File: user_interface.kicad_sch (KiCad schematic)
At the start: 31 parts, among them CN5 Line out, CN6 Headphone, J2 SWD, J3 I2C, J6 SPI, J9 Serial, P1 GPIO, SW4 BTN1, SW5 BTN2

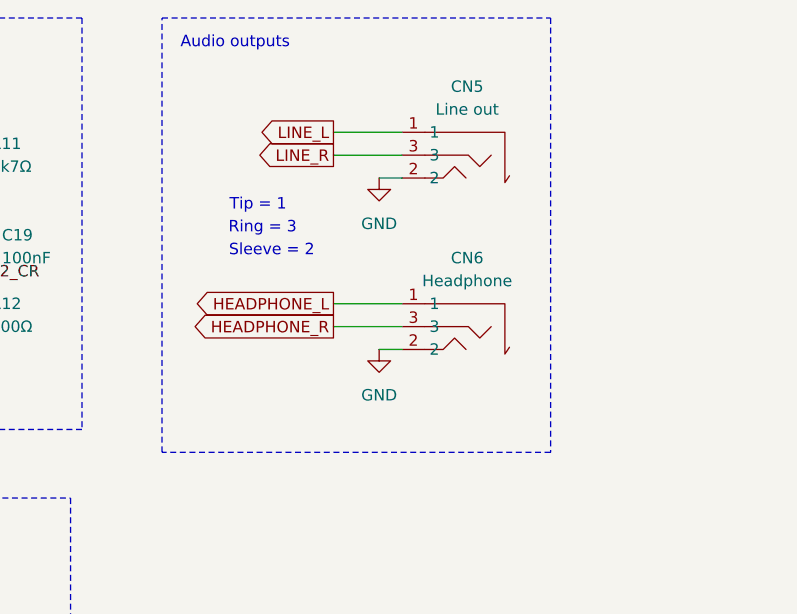
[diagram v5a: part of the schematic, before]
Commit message: Wire in headphone jack with 0-ohm
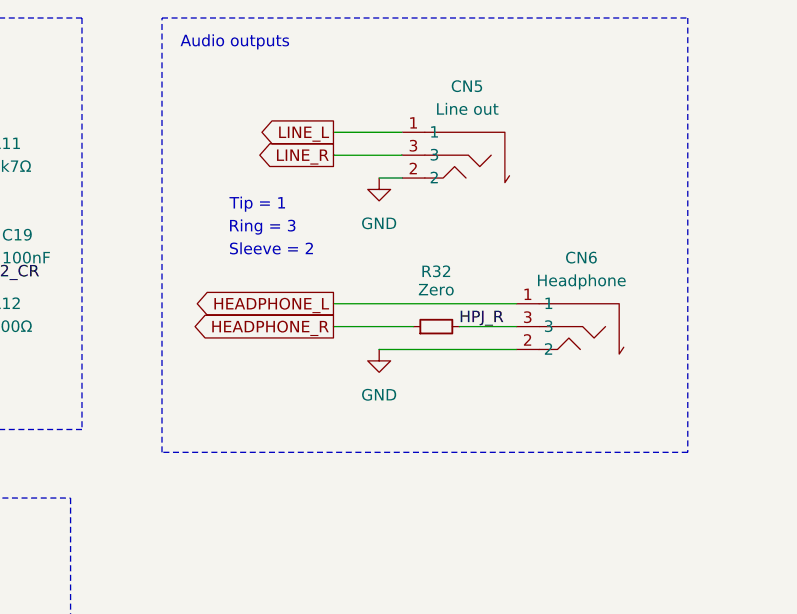
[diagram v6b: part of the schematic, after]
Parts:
- added R32: Zero, Resistor_SMD:R_2010_5025Metric, symbol Device:R_Small
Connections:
- net HEADPHONE_R: now also R32.1; no longer CN6.3
- new net HPJ_R: CN6.3, R32.2
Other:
- moved on the sheet: CN6
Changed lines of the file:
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@@
 	(wire
 		(pts
-			(xy 212.09 53.34) (xy 219.71 53.34)
+			(xy 212.09 53.34) (xy 220.98 53.34)
 		)
 		(stroke
@@
 	(wire
 		(pts
+			(xy 226.06 53.34) (xy 232.41 53.34)
+		)
+		(stroke
+			(width 0)
+			(type default)
+		)
+	)
+	(wire
+		(pts
 			(xy 68.58 175.26) (xy 74.93 175.26)
 		)
@@
 	(wire
 		(pts
-			(xy 212.09 50.8) (xy 219.71 50.8)
+			(xy 212.09 50.8) (xy 232.41 50.8)
 		)
 		(stroke
@@
 	(wire
 		(pts
-			(xy 217.17 55.88) (xy 219.71 55.88)
+			(xy 217.17 55.88) (xy 232.41 55.88)
 		)
 		(stroke
@@
 	(rectangle
 		(start 193.04 19.05)
-		(end 236.22 67.31)
+		(end 251.46 67.31)
 		(stroke
 			(width 0)
@@
 		)
 	)
+	(label "HPJ_R"
+		(at 226.06 53.34 0)
+		(fields_autoplaced yes)
+		(effects
+			(font
+				(size 1.27 1.27)
+			)
+			(justify left bottom)
+		)
+	)
 	(label "BTN2_CR"
 		(at 171.45 48.26 0)
@@
 	(symbol
 		(lib_id "easyeda2kicad:PJ-321A-4A")
-		(at 222.25 53.34 0)
+		(at 234.95 53.34 0)
 		(mirror y)
 		(unit 1)
@@
 		(dnp no)
 		(property "Reference" "CN6"
-			(at 226.95 45.72 0)
+			(at 239.65 45.72 0)
 			(effects
 				(font
@@
 		)
 		(property "Value" "Headphone"
-			(at 226.95 48.26 0)
+			(at 239.65 48.26 0)
 			(effects
 				(font
@@
 		)
 		(property "Footprint" "easyeda2kicad:AUDIO-SMD_PJ-321A-4A"
-			(at 222.25 63.5 0)
+			(at 234.95 63.5 0)
 			(effects
 				(font
@@
 		)
 		(property "Datasheet" "https://lcsc.com/product-detail/Audio-Video-Connectors_Korean-Hroparts-Elec-PJ-321A-4A_C879743.html"
-			(at 222.25 66.04 0)
+			(at 234.95 66.04 0)
 			(effects
 				(font
@@
 		)
 		(property "Description" "Korean Hroparts Elec PJ-321A-4A -20℃~+70℃ 3.5mm Headphone Jack 30V 500mA SMD Audio Connectors (Headphones) ROHS"
-			(at 222.25 53.34 0)
+			(at 234.95 53.34 0)
 			(effects
 				(font
@@
 		)
 		(property "LCSC Part" "C879743"
-			(at 222.25 68.58 0)
+			(at 234.95 68.58 0)
 			(effects
 				(font
@@
 		)
 		(property "LCSC" "C879743"
-			(at 222.25 53.34 0)
+			(at 234.95 53.34 0)
 			(effects
 				(font
@@
 		)
 		(property "DPFNOTES" "In-stock 3.5mm TRS"
-			(at 222.25 53.34 0)
+			(at 234.95 53.34 0)
 			(effects
 				(font
@@
 		)
 		(property "DPFURL" "https://jlcpcb.com/partdetail/Korean_HropartsElec-PJ_321A4A/C879743"
-			(at 222.25 53.34 0)
+			(at 234.95 53.34 0)
 			(effects
 				(font
@@
 					(unit 1)
 				)
+			)
+		)
+	)
+	(symbol
+		(lib_id "Device:R_Small")
+		(at 223.52 53.34 90)
+		(unit 1)
+		(exclude_from_sim no)
+		(in_bom yes)
+		(on_board yes)
+		(dnp no)
+		(property "Reference" "R32"
+			(at 223.52 47.244 90)
+			(effects
+				(font
+					(size 1.27 1.27)
+				)
+			)
+		)
+		(property "Value" "Zero"
+			(at 223.52 49.276 90)
+			(effects
+				(font
+					(size 1.27 1.27)
+				)
+			)
+		)
+		(property "Footprint" "Resistor_SMD:R_2010_5025Metric"
+			(at 223.52 53.34 0)
+			(effects
+				(font
+					(size 1.27 1.27)
+				)
+				(hide yes)
+			)
+		)
+		(property "Datasheet" "~"
+			(at 223.52 53.34 0)
+			(effects
+				(font
+					(size 1.27 1.27)
+				)
+				(hide yes)
+			)
+		)
+		(property "Description" "Resistor, small symbol"
+			(at 223.52 53.34 0)
+			(effects
+				(font
+					(size 1.27 1.27)
+				)
+				(hide yes)
+			)
+		)
+		(property "LCSC" ""
+			(at 223.52 53.34 0)
+			(effects
+				(font
+					(size 1.27 1.27)
+				)
+				(hide yes)
+			)
+		)
+		(property "DPFNOTES" "For Routing"
+			(at 223.52 53.34 0)
+			(effects
+				(font
+					(size 1.27 1.27)
+				)
+				(hide yes)
+			)
+		)
+		(property "DPFURL" ""
+			(at 223.52 53.34 0)
+			(effects
+				(font
+					(size 1.27 1.27)
+				)
+				(hide yes)
+			)
+		)
+		(pin "1"
+		)
+		(pin "2"
+		)
+		(instances
+			(project "stm-midi-poc1"
+				(path "/7cd74113-1f92-4dcc-8610-19aa9fc81e5f/96c396b4-5394-4a50-9288-ad4476d1492f"
+					(reference "R32")
+					(unit 1)
+				)

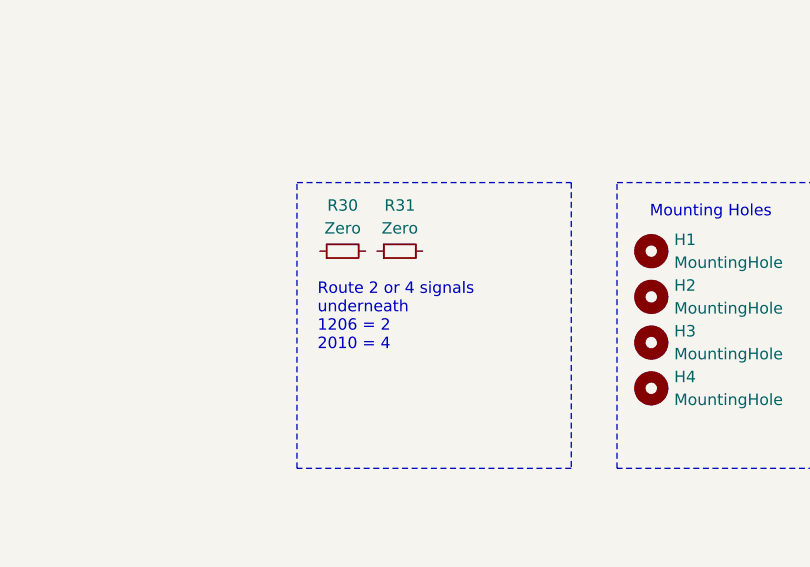
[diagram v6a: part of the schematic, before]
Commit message: Audio section is completely routed.
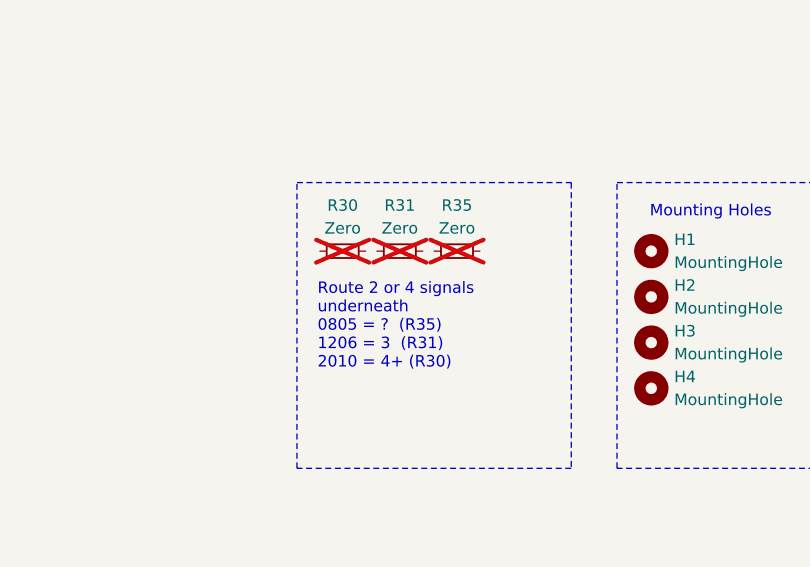
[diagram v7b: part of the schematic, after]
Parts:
- added R35: Zero, Resistor_SMD:R_0805_2012Metric, symbol Device:R_Small
- R30, R31: now not fitted; now left out of the parts list
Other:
- note added: "Route 2 or 4 signals underneath 0805 = ? (R35) 1206 = 3 (R31) 2010 = 4+ (R30)"
- note removed: "Route 2 or 4 signals underneath 1206 = 2 2010 = 4"
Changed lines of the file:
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@@
 		)
 	)
-	(text "Route 2 or 4 signals\nunderneath\n1206 = 2\n2010 = 4"
+	(text "Route 2 or 4 signals\nunderneath\n0805 = ?  (R35)\n1206 = 3  (R31)\n2010 = 4+ (R30)"
 		(exclude_from_sim no)
 		(at 197.866 145.796 0)
@@
 	)
 	(symbol
+		(lib_id "Device:R_Small")
+		(at 213.36 142.24 90)
+		(unit 1)
+		(exclude_from_sim yes)
+		(in_bom no)
+		(on_board no)
+		(dnp yes)
+		(property "Reference" "R35"
+			(at 213.36 137.16 90)
+			(effects
+				(font
+					(size 1.27 1.27)
+				)
+			)
+		)
+		(property "Value" "Zero"
+			(at 213.36 139.7 90)
+			(effects
+				(font
+					(size 1.27 1.27)
+				)
+			)
+		)
+		(property "Footprint" "Resistor_SMD:R_0805_2012Metric"
+			(at 213.36 142.24 0)
+			(effects
+				(font
+					(size 1.27 1.27)
+				)
+				(hide yes)
+			)
+		)
+		(property "Datasheet" "~"
+			(at 213.36 142.24 0)
+			(effects
+				(font
+					(size 1.27 1.27)
+				)
+				(hide yes)
+			)
+		)
+		(property "Description" "Resistor, small symbol"
+			(at 213.36 142.24 0)
+			(effects
+				(font
+					(size 1.27 1.27)
+				)
+				(hide yes)
+			)
+		)
+		(property "LCSC" ""
+			(at 213.36 142.24 0)
+			(effects
+				(font
+					(size 1.27 1.27)
+				)
+				(hide yes)
+			)
+		)
+		(property "DPFNOTES" "For Routing"
+			(at 213.36 142.24 0)
+			(effects
+				(font
+					(size 1.27 1.27)
+				)
+				(hide yes)
+			)
+		)
+		(property "DPFURL" ""
+			(at 213.36 142.24 0)
+			(effects
+				(font
+					(size 1.27 1.27)
+				)
+				(hide yes)
+			)
+		)
+		(pin "1"
+		)
+		(pin "2"
+		)
+		(instances
+			(project "stm-midi-poc1"
+				(path "/7cd74113-1f92-4dcc-8610-19aa9fc81e5f/96c396b4-5394-4a50-9288-ad4476d1492f"
+					(reference "R35")
+					(unit 1)
+				)
+			)
+		)
+	)
+	(symbol
 		(lib_id "Device:LED")
 		(at 81.28 38.1 90)
@@
 		(at 207.01 142.24 90)
 		(unit 1)
-		(exclude_from_sim no)
-		(in_bom yes)
-		(on_board yes)
-		(dnp no)
+		(exclude_from_sim yes)
+		(in_bom no)
+		(on_board no)
+		(dnp yes)
 		(property "Reference" "R31"
 			(at 207.01 137.16 90)
@@
 		(at 200.66 142.24 90)
 		(unit 1)
-		(exclude_from_sim no)
-		(in_bom yes)
-		(on_board yes)
-		(dnp no)
+		(exclude_from_sim yes)
+		(in_bom no)
+		(on_board no)
+		(dnp yes)
 		(fields_autoplaced yes)
 		(property "Reference" "R30"

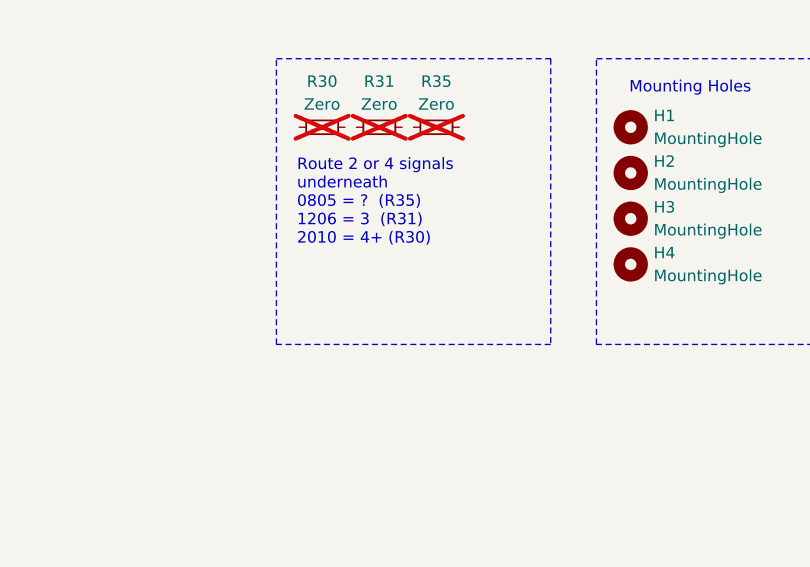
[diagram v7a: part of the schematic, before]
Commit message: Routed the SWD. I don't think it will be possible to do this on a 2-layer board anymore. I already had to use several 0-ohm resistors.
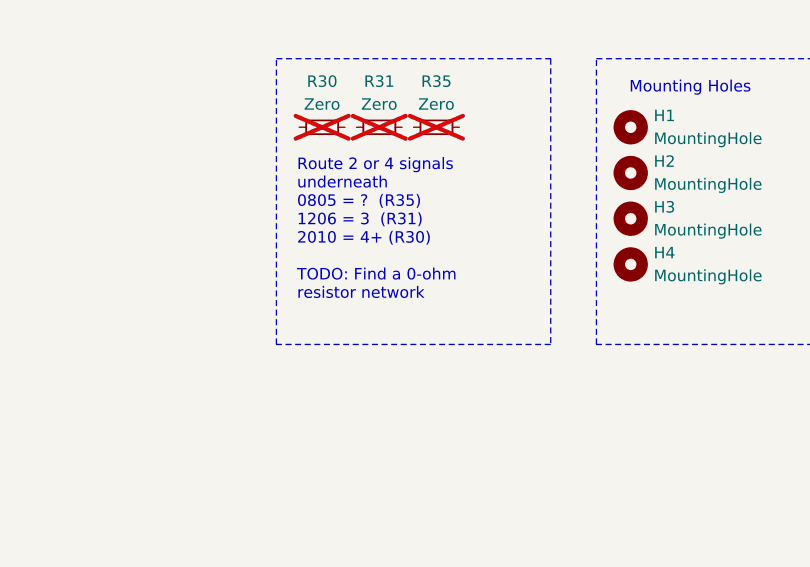
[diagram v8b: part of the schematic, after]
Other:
- note added: "Route 2 or 4 signals underneath 0805 = ? (R35) 1206 = 3 (R31) 2010 = 4+ (R30) TODO: Find a 0-ohm resistor network"
- note removed: "Route 2 or 4 signals underneath 0805 = ? (R35) 1206 = 3 (R31) 2010 = 4+ (R30)"
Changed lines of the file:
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@@
 		)
 	)
-	(text "Route 2 or 4 signals\nunderneath\n0805 = ?  (R35)\n1206 = 3  (R31)\n2010 = 4+ (R30)"
+	(text "Route 2 or 4 signals\nunderneath\n0805 = ?  (R35)\n1206 = 3  (R31)\n2010 = 4+ (R30)\n\nTODO: Find a 0-ohm\nresistor network"
 		(exclude_from_sim no)
 		(at 197.866 145.796 0)
